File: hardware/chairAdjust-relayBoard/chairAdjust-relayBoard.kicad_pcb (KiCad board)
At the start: 2 copper layers, 101 x 78.7 mm, 51 parts, among them J1 Motor_1 + -, J2 Control-Signals, J3 Control-Signals, J4 24V Power, J5 GND Power, J6 12V, GND, J7 Motor_2 + -, K1 RT314A24, K2 RT314A24, K3 RT314A24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

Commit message: pcb: remove gnd tracks, export, generate gcode
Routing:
- net GNDPWR: track 162.3 -> 39.1 mm
- net GND: track 101.2 -> 0.00 mm

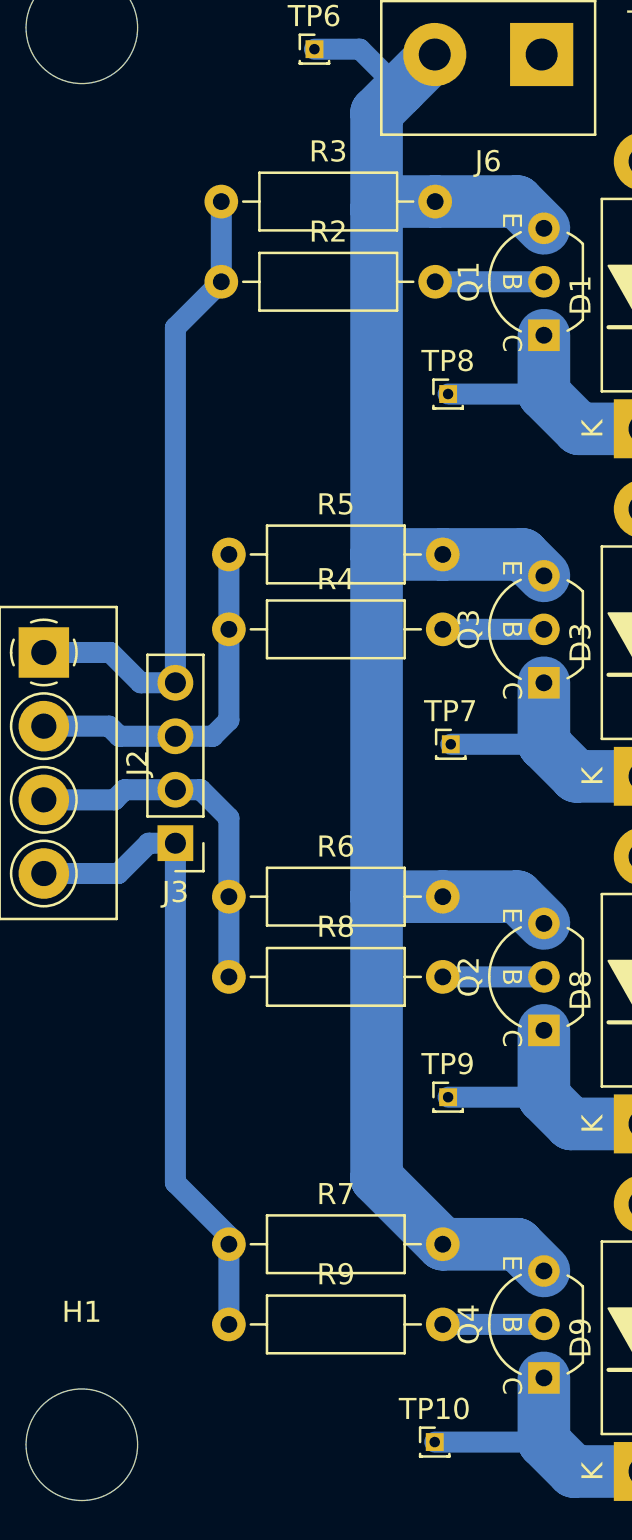
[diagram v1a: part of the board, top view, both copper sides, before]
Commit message: pcb: add 3d-model, exports
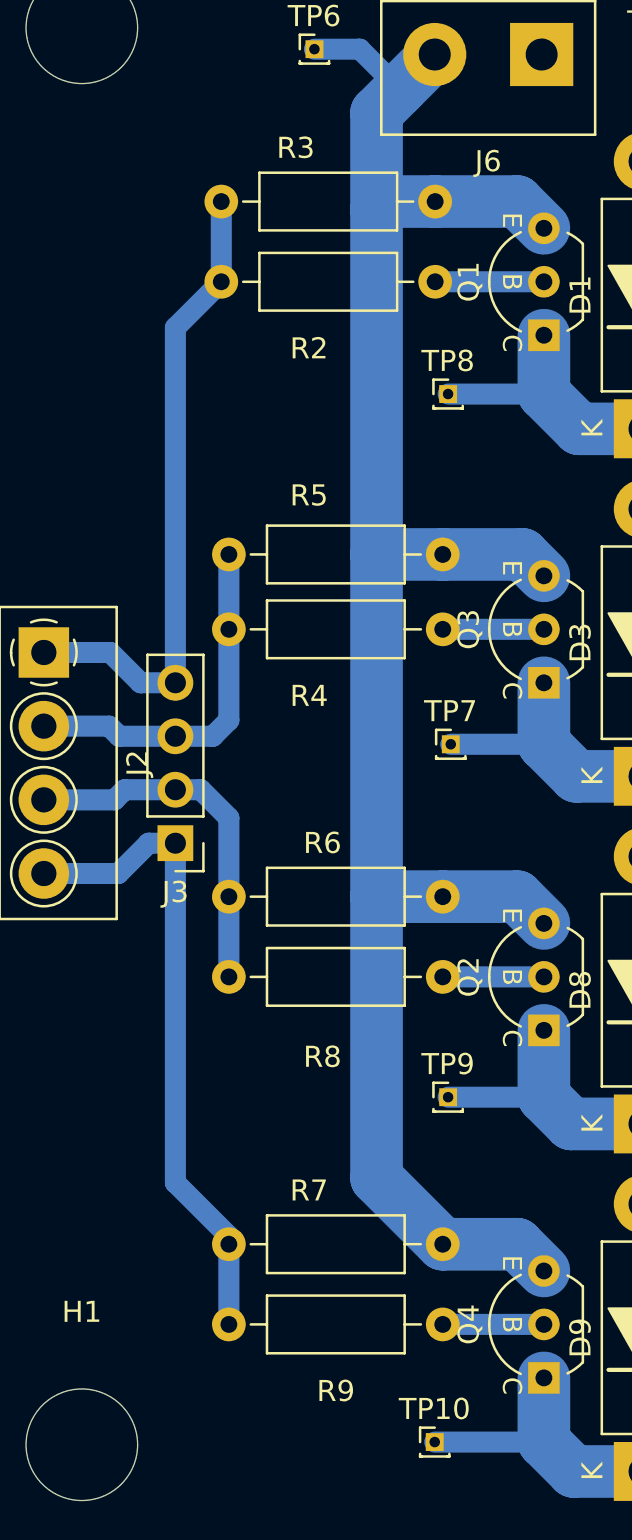
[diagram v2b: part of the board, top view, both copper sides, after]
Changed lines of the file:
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@@
 			(pintype "passive")
 		)
-		(model "${KICAD8_3DMODEL_DIR}/TerminalBlock.3dshapes/TerminalBlock_bornier-2_P5.08mm.wrl"
+		(model "${KICAD8_3DMODEL_DIR}/TerminalBlock_Phoenix.3dshapes/TerminalBlock_Phoenix_PT-1,5-2-5.0-H_1x02_P5.00mm_Horizontal.step"
 			(offset
-				(xyz 2.539999962 0 0)
+				(xyz 0 0 0)
 			)
 			(scale
@@
 			(pintype "passive")
 		)
+		(model "${KICAD8_3DMODEL_DIR}/Diode_THT.3dshapes/D_A-405_P12.70mm_Horizontal.wrl"
+			(offset
+				(xyz 0 0 0)
+			)
+			(scale
+				(xyz 1.6 2 2)
+			)
+			(rotate
+				(xyz 0 0 0)
+			)
+		)
 	)
 	(footprint "Resistor_THT:R_Axial_DIN0207_L6.3mm_D2.5mm_P10.16mm_Horizontal"
@@
 		(tags "Resistor Axial_DIN0207 series Axial Horizontal pin pitch 10.16mm 0.25W = 1/4W length 6.3mm diameter 2.5mm")
 		(property "Reference" "R7"
-			(at 5.08 -2.37 0)
+			(at 3.81 -2.54 0)
 			(layer "F.SilkS")
 			(effects
@@
 		)
 		(property "Value" "22k"
-			(at 5.08 2.37 0)
+			(at 5.08 0 0)
 			(layer "F.Fab")
 			(effects
@@
 		)
 		(fp_text user "${REFERENCE}"
-			(at 5.08 0 0)
+			(at 3.81 -2.54 0)
 			(layer "F.Fab")
 			(effects
@@
 			(pintype "passive")
 		)
+		(model "${KICAD8_3DMODEL_DIR}/Diode_THT.3dshapes/D_A-405_P12.70mm_Horizontal.wrl"
+			(offset
+				(xyz 0 0 0)
+			)
+			(scale
+				(xyz 1.6 2 2)
+			)
+			(rotate
+				(xyz 0 0 0)
+			)
+		)
 	)
 	(footprint "Connector_PinHeader_1.00mm:PinHeader_1x01_P1.00mm_Vertical"
@@
 			(pintype "passive")
 		)
+		(model "${KICAD8_3DMODEL_DIR}/Diode_THT.3dshapes/D_A-405_P12.70mm_Horizontal.wrl"
+			(offset
+				(xyz 0 0 0)
+			)
+			(scale
+				(xyz 1.6 2 2)
+			)
+			(rotate
+				(xyz 0 0 0)
+			)
+		)
 	)
 	(footprint "Diode_THT_AKL_Double:D_DO-27_P20.32mm_Horizontal"
@@
 			(pintype "passive")
 		)
+		(model "${KICAD8_3DMODEL_DIR}/Diode_THT.3dshapes/D_A-405_P12.70mm_Horizontal.wrl"
+			(offset
+				(xyz 0 0 0)
+			)
+			(scale
+				(xyz 1.6 2 2)
+			)
+			(rotate
+				(xyz 0 0 0)
+			)
+		)
 	)
 	(footprint "Package_TO_SOT_THT_AKL:TO-92_Inline_Wide_CBE"
@@
 		)
 		(property "Value" "Motor_2 +  -"
-			(at 2.54 5.08 90)
+			(at 2.54 5.715 90)
 			(layer "F.Fab")
 			(effects
@@
 			(pintype "passive")
 		)
-		(model "${KICAD8_3DMODEL_DIR}/TerminalBlock.3dshapes/TerminalBlock_bornier-2_P5.08mm.wrl"
+		(model "${KICAD8_3DMODEL_DIR}/TerminalBlock_Phoenix.3dshapes/TerminalBlock_Phoenix_PT-1,5-2-5.0-H_1x02_P5.00mm_Horizontal.step"
 			(offset
-				(xyz 2.539999962 0 0)
+				(xyz 0 0 0)
 			)
 			(scale
@@
 		)
 		(property "Value" "Control-Signals"
-			(at 0 9.95 0)
+			(at 10.795 3.81 90)
 			(layer "F.Fab")
 			(effects
@@
 		)
 		(property "Value" "Motor_1 +  -"
-			(at 2.54 5.08 90)
+			(at 2.54 5.715 90)
 			(layer "F.Fab")
 			(effects
@@
 			(pintype "passive")
 		)
-		(model "${KICAD8_3DMODEL_DIR}/TerminalBlock.3dshapes/TerminalBlock_bornier-2_P5.08mm.wrl"
+		(model "${KICAD8_3DMODEL_DIR}/TerminalBlock_Phoenix.3dshapes/TerminalBlock_Phoenix_PT-1,5-2-5.0-H_1x02_P5.00mm_Horizontal.step"
 			(offset
-				(xyz 2.539999962 0 0)
+				(xyz 0 0 0)
 			)
 			(scale
@@
 		(tags "Resistor Axial_DIN0207 series Axial Horizontal pin pitch 10.16mm 0.25W = 1/4W length 6.3mm diameter 2.5mm")
 		(property "Reference" "R2"
-			(at 5.08 -2.37 0)
+			(at 4.17 3.175 0)
 			(layer "F.SilkS")
 			(effects
@@
 		)
 		(property "Value" "2k2"
-			(at 5.08 2.37 0)
+			(at 4.17 0 0)
 			(layer "F.Fab")
 			(effects
@@
 		)
 		(fp_text user "${REFERENCE}"
-			(at 5.08 0 0)
+			(at 4.17 3.175 0)
 			(layer "F.Fab")
 			(effects
@@
 			(pintype "passive")
 		)
+		(model "${KICAD8_3DMODEL_DIR}/Diode_THT.3dshapes/D_A-405_P12.70mm_Horizontal.wrl"
+			(offset
+				(xyz 0 0 0)
+			)
+			(scale
+				(xyz 1.6 2 2)
+			)
+			(rotate
+				(xyz 0 0 0)
+			)
+		)
 	)
 	(footprint "Connector_PinHeader_1.00mm:PinHeader_1x01_P1.00mm_Vertical"
@@
 		)
 		(property "Value" "Control-Signals"
-			(at 5.25 4.66 90)
+			(at -0.465 5.815 90)
 			(layer "F.Fab")
+			(hide yes)
 			(effects
 				(font
@@
 			(pintype "passive")
 		)
-		(model "${KICAD8_3DMODEL_DIR}/TerminalBlock_4Ucon.3dshapes/TerminalBlock_4Ucon_1x04_P3.50mm_Horizontal.wrl"
+		(model "${KICAD8_3DMODEL_DIR}/TerminalBlock_Phoenix.3dshapes/TerminalBlock_Phoenix_PT-1,5-4-3.5-H_1x04_P3.50mm_Horizontal.step"
 			(offset
 				(xyz 0 0 0)
@@
 			(pintype "passive")
 		)
+		(model "${KICAD8_3DMODEL_DIR}/Diode_THT.3dshapes/D_A-405_P12.70mm_Horizontal.wrl"
+			(offset
+				(xyz 0.2 0 0)
+			)
+			(scale
+				(xyz 1.6 2 2)
+			)
+			(rotate
+				(xyz 0 0 0)
+			)
+		)
 	)
 	(footprint "Diode_THT_AKL:D_5W_P12.70mm_Horizontal"
@@
 		(tags "Resistor Axial_DIN0207 series Axial Horizontal pin pitch 10.16mm 0.25W = 1/4W length 6.3mm diameter 2.5mm")
 		(property "Reference" "R5"
-			(at 5.08 -2.37 0)
+			(at 3.81 -2.794 0)
 			(layer "F.SilkS")
 			(effects
@@
 		)
 		(property "Value" "22k"
-			(at 5.08 2.37 0)
+			(at 3.81 -0.254 0)
 			(layer "F.Fab")
 			(effects
@@
 		)
 		(fp_text user "${REFERENCE}"
-			(at 5.08 0 0)
+			(at 3.81 -2.794 0)
 			(layer "F.Fab")
 			(effects
@@
 			(pintype "passive")
 		)
+		(model "${KICAD8_3DMODEL_DIR}/Diode_THT.3dshapes/D_A-405_P12.70mm_Horizontal.wrl"
+			(offset
+				(xyz 0 0 0)
+			)
+			(scale
+				(xyz 1.6 2 2)
+			)
+			(rotate
+				(xyz 0 0 0)
+			)
+		)
 	)
 	(footprint "Resistor_THT:R_Axial_DIN0207_L6.3mm_D2.5mm_P10.16mm_Horizontal"
@@
 		(tags "Resistor Axial_DIN0207 series Axial Horizontal pin pitch 10.16mm 0.25W = 1/4W length 6.3mm diameter 2.5mm")
 		(property "Reference" "R4"
-			(at 5.08 -2.37 0)
+			(at 3.81 3.175 0)
 			(layer "F.SilkS")
 			(effects
@@
 		)
 		(property "Value" "2k2"
-			(at 5.08 2.37 0)
+			(at 3.81 0 0)
 			(layer "F.Fab")
 			(effects
@@
 		)
 		(fp_text user "${REFERENCE}"
-			(at 5.08 0 0)
+			(at 3.81 3.175 0)
 			(layer "F.Fab")
 			(effects
@@
 			(pintype "passive")
 		)
-		(model "${KICAD8_3DMODEL_DIR}/TerminalBlock.3dshapes/TerminalBlock_bornier-2_P5.08mm.wrl"
+		(model "${KICAD8_3DMODEL_DIR}/TerminalBlock_Phoenix.3dshapes/TerminalBlock_Phoenix_PT-1,5-2-5.0-H_1x02_P5.00mm_Horizontal.step"
 			(offset
-				(xyz 2.539999962 0 0)
+				(xyz 0 0 0)
 			)
 			(scale
@@
 		(tags "Resistor Axial_DIN0207 series Axial Horizontal pin pitch 10.16mm 0.25W = 1/4W length 6.3mm diameter 2.5mm")
 		(property "Reference" "R3"
-			(at 5.08 -2.37 0)
+			(at 3.535 -2.54 0)
 			(layer "F.SilkS")
 			(effects
@@
 		)
 		(property "Value" "22k"
-			(at 5.08 2.37 0)
+			(at 3.535 0 0)
 			(layer "F.Fab")
 			(effects
@@
 		)
 		(fp_text user "${REFERENCE}"
-			(at 5.08 0 0)
+			(at 3.535 -2.54 0)
 			(layer "F.Fab")
 			(effects
@@
 			(pintype "passive")
 		)
+		(model "${KICAD8_3DMODEL_DIR}/Diode_THT.3dshapes/D_A-405_P12.70mm_Horizontal.wrl"
+			(offset
+				(xyz 0 0 0)
+			)
+			(scale
+				(xyz 1.6 2 2)
+			)
+			(rotate
+				(xyz 0 0 0)
+			)
+		)
 	)
 	(footprint "Resistor_THT:R_Axial_DIN0207_L6.3mm_D2.5mm_P10.16mm_Horizontal"
@@
 		(tags "Resistor Axial_DIN0207 series Axial Horizontal pin pitch 10.16mm 0.25W = 1/4W length 6.3mm diameter 2.5mm")
 		(property "Reference" "R6"
-			(at 5.08 -2.37 0)
+			(at 4.445 -2.54 0)
 			(layer "F.SilkS")
 			(effects
@@
 		)
 		(property "Value" "22k"
-			(at 5.08 2.37 0)
+			(at 3.81 0 0)
 			(layer "F.Fab")
 			(effects
@@
 		)
 		(fp_text user "${REFERENCE}"
-			(at 5.08 0 0)
+			(at 4.445 -2.54 0)
 			(layer "F.Fab")
 			(effects
@@
 			(pintype "passive")
 		)
-		(model "${KICAD8_3DMODEL_DIR}/TerminalBlock.3dshapes/TerminalBlock_bornier-2_P5.08mm.wrl"
+		(model "${KICAD8_3DMODEL_DIR}/TerminalBlock_Phoenix.3dshapes/TerminalBlock_Phoenix_PT-1,5-2-5.0-H_1x02_P5.00mm_Horizontal.step"
 			(offset
-				(xyz 2.539999962 0 0)
+				(xyz 0 0 0)
 			)
 			(scale
@@
 		(tags "Resistor Axial_DIN0207 series Axial Horizontal pin pitch 10.16mm 0.25W = 1/4W length 6.3mm diameter 2.5mm")
 		(property "Reference" "R9"
-			(at 5.08 -2.37 0)
+			(at 5.08 3.175 0)
 			(layer "F.SilkS")
 			(effects
@@
 		)
 		(property "Value" "2k2"
-			(at 5.08 2.37 0)
+			(at 5.08 0 0)
 			(layer "F.Fab")
 			(effects
@@
 		)
 		(fp_text user "${REFERENCE}"
-			(at 5.08 0 0)
+			(at 5.08 3.175 0)
 			(layer "F.Fab")
 			(effects
@@
 		(tags "Resistor Axial_DIN0207 series Axial Horizontal pin pitch 10.16mm 0.25W = 1/4W length 6.3mm diameter 2.5mm")
 		(property "Reference" "R8"
-			(at 5.08 -2.37 0)
+			(at 4.445 3.81 0)
 			(layer "F.SilkS")
 			(effects
@@
 		)
 		(property "Value" "2k2"
-			(at 5.08 2.37 0)
+			(at 3.81 0 0)
 			(layer "F.Fab")
 			(effects
@@
 		)
 		(fp_text user "${REFERENCE}"
-			(at 5.08 0 0)
+			(at 4.445 3.81 0)
 			(layer "F.Fab")
 			(effects
@@
 		(layer "Edge.Cuts")
 	)
-	(dimension
-		(type aligned)
-		(layer "User.8")
-		(pts
-			(xy 208.28 28.575) (xy 208.28 107.315)
-		)
-		(height -13.97)
-		(gr_text "78.7400 mm"
-			(at 221.1 67.945 90)
-			(layer "User.8")
-			(effects
-				(font
-					(size 1 1)
-					(thickness 0.15)
-				)
-			)
-		)
-		(format
-			(prefix "")
-			(suffix "")
-			(units 3)
-			(units_format 1)
-			(precision 4)
-		)
-		(style
-			(thickness 0.1)
-			(arrow_length 1.27)
-			(text_position_mode 0)
-			(extension_height 0.58642)
-			(extension_offset 0.5) keep_text_aligned)
-	)
-	(dimension
-		(type aligned)
-		(layer "User.8")
-		(pts
-			(xy 208.28 107.315) (xy 107.315 107.315)
-		)
-		(height -8.89)
-		(gr_text "100.9650 mm"
-			(at 157.7975 115.055 0)
-			(layer "User.8")
-			(effects
-				(font
-					(size 1 1)
-					(thickness 0.15)
-				)
-			)
-		)
-		(format
-			(prefix "")
-			(suffix "")
-			(units 3)
-			(units_format 1)
-			(precision 4)
-		)
-		(style
-			(thickness 0.1)
-			(arrow_length 1.27)
-			(text_position_mode 0)
-			(extension_height 0.58642)
-			(extension_offset 0.5) keep_text_aligned)
-	)
 	(segment
